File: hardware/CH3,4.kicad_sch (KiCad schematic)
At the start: 104 parts, among them J2 RJ45, J3 RJ45, U10 ADG719, U11 INA828, U12 OPA2192, U13 OPA2192, U14 INA828, U15 SGM2059, U4 INA828, U5 OPA2192, U6 OPA2192, U7 INA828, U8 SGM2059, U9 ADG719

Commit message: feat：远程感测原理图；多路通道
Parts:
- removed C136, C137, C27, C28, C33, C34: 1uF, Capacitor_SMD:C_0603_1608Metric, symbol Device:C
- removed C20, C30: 120pF, Capacitor_SMD:C_0603_1608Metric, symbol Device:C
- removed C21, C22, C24, C25, C26, C29, C31, C35, C36, C37: 100pF, Capacitor_SMD:C_0603_1608Metric, symbol Device:C
- removed C23, C32: 750pF, Capacitor_SMD:C_0603_1608Metric, symbol Device:C
- removed C44, C47, C58, C59, C60, C61, C62, C63, C64, C65, C66, C67, C68, C69, C70, C72, C74, C76, C81, C83: 10uF, Capacitor_SMD:C_0603_1608Metric, symbol Device:C
- removed C45, C46, C48, C49, C50, C51, C52, C53, C54, C55, C56, C57, C71, C73, C75, C77, C78, C79, C80, C82: 100nF, Capacitor_SMD:C_0603_1608Metric, symbol Device:C
- removed J2, J3: RJ45, Connector_RJ:RJ45_Amphenol_54602-x08_Horizontal, symbol Connector:RJ45
- removed R10, R27: 8kR, Resistor_SMD:R_0603_1608Metric, symbol Device:R
- removed R11, R25: 7kR, Resistor_SMD:R_0603_1608Metric, symbol Device:R
- removed R12, R14, R18, R19, R26, R28, R3, R4: 1kR, Resistor_SMD:R_0603_1608Metric, symbol Device:R
- removed R13, R31: 26.7kR, Resistor_SMD:R_0603_1608Metric, symbol Device:R
- removed R15, R16, R29, R30: 49.9R, Resistor_SMD:R_0603_1608Metric, symbol Device:R
- removed R17, R32: 12.4kR, Resistor_SMD:R_0603_1608Metric, symbol Device:R
- removed R20, R5: 120R, Resistor_SMD:R_0603_1608Metric, symbol Device:R
- removed R21, R7: 6.19kR, Resistor_SMD:R_0603_1608Metric, symbol Device:R
- removed R22, R6: 8.45kR, Resistor_SMD:R_0603_1608Metric, symbol Device:R
- removed R23, R8: 2.15kR, Resistor_SMD:R_0603_1608Metric, symbol Device:R
- removed R24, R9: 3.92kR, Resistor_SMD:R_0603_1608Metric, symbol Device:R
- removed U10, U9: ADG719, ProPrj_New Project_2026-05-28_15-29-15_2026-05-30:SOT-23-8_L3.0-W1.7-P0.65-LS2.8-TL, symbol Analog_Switch:ADG619BRTZ-REEL7
- removed U11, U14, U4, U7: INA828, Package_SO:Infineon_PG-DSO-8-43, symbol Amplifier_Instrumentation:INA828IDR
- removed U12, U13, U5, U6: OPA2192, Package_SO:SOIC-8_3.9x4.9mm_P1.27mm, symbol Amplifier_Operational:OPA2192IDR
- removed U15, U8: SGM2059, Package_TO_SOT_SMD:SOT-23-5, symbol Regulator_Linear:SGM2059-ADJXN5G/TR
- added C100, C103, C104, C106, C109, C110, C111, C112, C113, C114, C115, C116, C117, C118, C120, C121, C122, C123, C86, C98: 100nF, Capacitor_SMD:C_0603_1608Metric, symbol Device:C
- added C101, C102, C105, C107, C108, C119, C84, C85, C87, C88, C89, C90, C91, C92, C93, C94, C95, C96, C97, C99: 10uF, Capacitor_SMD:C_0603_1608Metric, symbol Device:C
- added C124, C125: 750pF, Capacitor_SMD:C_0603_1608Metric, symbol Device:C
- added C126, C127, C131, C132, C138, C139: 1uF, Capacitor_SMD:C_0603_1608Metric, symbol Device:C
- added C128, C129, C130, C133, C134, C135, C38, C39, C42, C43: 100pF, Capacitor_SMD:C_0603_1608Metric, symbol Device:C
- added C40, C41: 120pF, Capacitor_SMD:C_0603_1608Metric, symbol Device:C
- added J4, J5: RJ45, Connector_RJ:RJ45_Amphenol_54602-x08_Horizontal, symbol Connector:RJ45
- added R33, R41: 26.7kR, Resistor_SMD:R_0603_1608Metric, symbol Device:R
- added R34, R35, R36, R37, R52, R54, R61, R62: 1kR, Resistor_SMD:R_0603_1608Metric, symbol Device:R
- added R38, R43: 12.4kR, Resistor_SMD:R_0603_1608Metric, symbol Device:R
- added R39, R40: 120R, Resistor_SMD:R_0603_1608Metric, symbol Device:R
- added R42, R44: 6.19kR, Resistor_SMD:R_0603_1608Metric, symbol Device:R
- added R45, R46: 8.45kR, Resistor_SMD:R_0603_1608Metric, symbol Device:R
- added R47, R48: 2.15kR, Resistor_SMD:R_0603_1608Metric, symbol Device:R
- added R49, R50: 3.92kR, Resistor_SMD:R_0603_1608Metric, symbol Device:R
- added R51, R53: 7kR, Resistor_SMD:R_0603_1608Metric, symbol Device:R
- added R55, R56, R59, R60: 49.9R, Resistor_SMD:R_0603_1608Metric, symbol Device:R
- added R57, R58: 8kR, Resistor_SMD:R_0603_1608Metric, symbol Device:R
- added U16, U20, U21, U22: INA828, Package_SO:Infineon_PG-DSO-8-43, symbol Amplifier_Instrumentation:INA828IDR
- added U17, U23: SGM2059, Package_TO_SOT_SMD:SOT-23-5, symbol Regulator_Linear:SGM2059-ADJXN5G/TR
- added U18, U19: ADG719, ProPrj_New Project_2026-05-28_15-29-15_2026-05-30:SOT-23-8_L3.0-W1.7-P0.65-LS2.8-TL, symbol Analog_Switch:ADG619BRTZ-REEL7
- added U24, U25, U26, U27: OPA2192, Package_SO:SOIC-8_3.9x4.9mm_P1.27mm, symbol Amplifier_Operational:OPA2192IDR
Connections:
- net +2.5VA: now also C138.2, C139.2, R34.1, R35.1
- net +4VA: now also C101.2, C102.1, C105.1, C108.1, C110.2, C112.2, C114.2, C115.1, C116.2, C117.2, C118.1, C119.2, C120.2, C121.1, C122.2, C123.1, C84.1, C87.1, C90.1, C92.1, C94.1, C96.1, C98.2, C99.1, U16.7 (+VS), U17.1 (IN), U17.3 (EN), U18.4 (VDD), U19.4 (VDD), U20.7 (+VS), U21.7 (+VS), U22.7 (+VS), U23.1 (IN), U23.3 (EN), U24.4 (VSS), U25.4 (VSS), U26.4 (VSS), U27.4 (VSS)
- net -4VA: now also C100.1, C103.1, C106.1, C109.1, C111.1, C113.1, C85.2, C88.2, C91.2, C93.2, C95.2, C97.2, U16.4 (-VS), U18.7 (VSS), U19.7 (VSS), U20.4 (-VS), U21.4 (-VS), U22.4 (-VS)
- net GND: now also C100.2, C101.1, C102.2, C103.2, C104.1, C105.2, C106.2, C107.1, C108.2, C109.2, C110.1, C111.2, C112.1, C113.2, C114.1, C115.2, C116.1, C117.1, C118.2, C119.1, C120.1, C121.2, C122.1, C123.2, C126.2, C127.2, C128.1, C130.2, C131.2, C132.2, C133.1, C135.2, C138.1, C139.1, C38.2, C39.2, C42.2, C43.2, C84.2, C85.1, C86.1, C87.2, C88.1, C89.1, C90.2, C91.1, C92.2, C93.1, C94.2, C95.1, C96.2, C97.1, C98.1, C99.2, J4.2, J4.7, J5.2, J5.7, R36.2, R37.2, R38.1, R43.1, U16.5 (REF), U17.2 (GND), U18.3 (GND), U19.3 (GND), U20.5 (REF), U23.2 (GND), U24.8 (VDD), U25.8 (VDD), U26.8 (VDD), U27.8 (VDD)
- net V_{REF}: now also C126.1, C127.1, C131.1, C132.1, R52.1, R54.1, U21.5 (REF), U22.5 (REF), U26.5 (VINB+), U27.5 (VINB+)
- new net: C40.2, R42.1, R45.2
- new net: R42.2, U21.6 (OUT)
- new net: R33.1, U16.6 (OUT)
- new net: R39.2, U21.1 (RG)
- new net: U18.1 (D), U21.2 (-IN)
- new net: R39.1, U21.8 (RG)
- new net: R58.1, R62.2, U27.6 (VINB-)
- new net: C38.1, R45.1, U24.3 (VINA+)
- new net: R40.2, U22.1 (RG)
- new net: U19.1 (D), U22.2 (-IN)
- new net: R44.2, U22.6 (OUT)
- new net: R40.1, U22.8 (RG)
- new net: R34.2, R36.1, U18.8 (S2)
- new net: C43.1, R50.1, U25.5 (VINB+)
- new net: C125.1, R53.2, R58.2, U25.6 (VINB-), U25.7 (VOUTB)
- new net: R57.1, R61.2, U26.6 (VINB-)
- new net: C124.1, R51.2, R57.2, U24.6 (VINB-), U24.7 (VOUTB)
- new net: C42.1, R49.1, U24.5 (VINB+)
- new net: R51.1, R52.2, U26.3 (VINA+)
- new net: R41.1, U20.6 (OUT)
- new net: R41.2, R43.2, U23.4 (FB)
- new net: R53.1, R54.2, U27.3 (VINA+)
- new net: C125.2, R48.1, R50.2
- new net: C39.1, R46.1, U25.3 (VINA+)
- new net: C41.2, R44.1, R46.2
- new net: C124.2, R47.1, R49.2
- new net: C41.1, R48.2, U25.1 (VOUTA), U25.2 (VINA-)
- new net: C40.1, R47.2, U24.1 (VOUTA), U24.2 (VINA-)
- new net: R33.2, R38.2, U17.4 (FB)
- new net: R35.2, R37.1, U19.8 (S2)
- new net CH3+: J4.4, U21.3 (+IN)
- new net CH3-: J4.5, U18.2 (S1)
- new net CH4+: J5.4, U22.3 (+IN)
- new net CH4-: J5.5, U19.2 (S1)
- new net Ctrl3: U18.6 (IN)
- new net Ctrl4: U19.6 (IN)
- new net D3Q+: R55.2, U26.1 (VOUTA), U26.2 (VINA-)
- new net D3Q-: R56.2, R61.1, U26.7 (VOUTB)
- new net D4Q+: R59.2, U27.1 (VOUTA), U27.2 (VINA-)
- new net D4Q-: R60.2, R62.1, U27.7 (VOUTB)
- new net EX3+: C86.2, C89.2, J4.1, J4.8, U17.5 (OUT)
- new net EX4+: C104.2, C107.2, J5.1, J5.8, U23.5 (OUT)
- new net OUT3+: C128.2, C129.1, R55.1
- new net OUT3-: C129.2, C130.1, R56.1
- new net OUT4+: C133.2, C134.1, R59.1
- new net OUT4-: C134.2, C135.1, R60.1
- new net RS3+: J4.3, U16.3 (+IN)
- new net RS3-: J4.6, U16.2 (-IN)
- new net RS4+: J5.3, U20.3 (+IN)
- new net RS4-: J5.6, U20.2 (-IN)

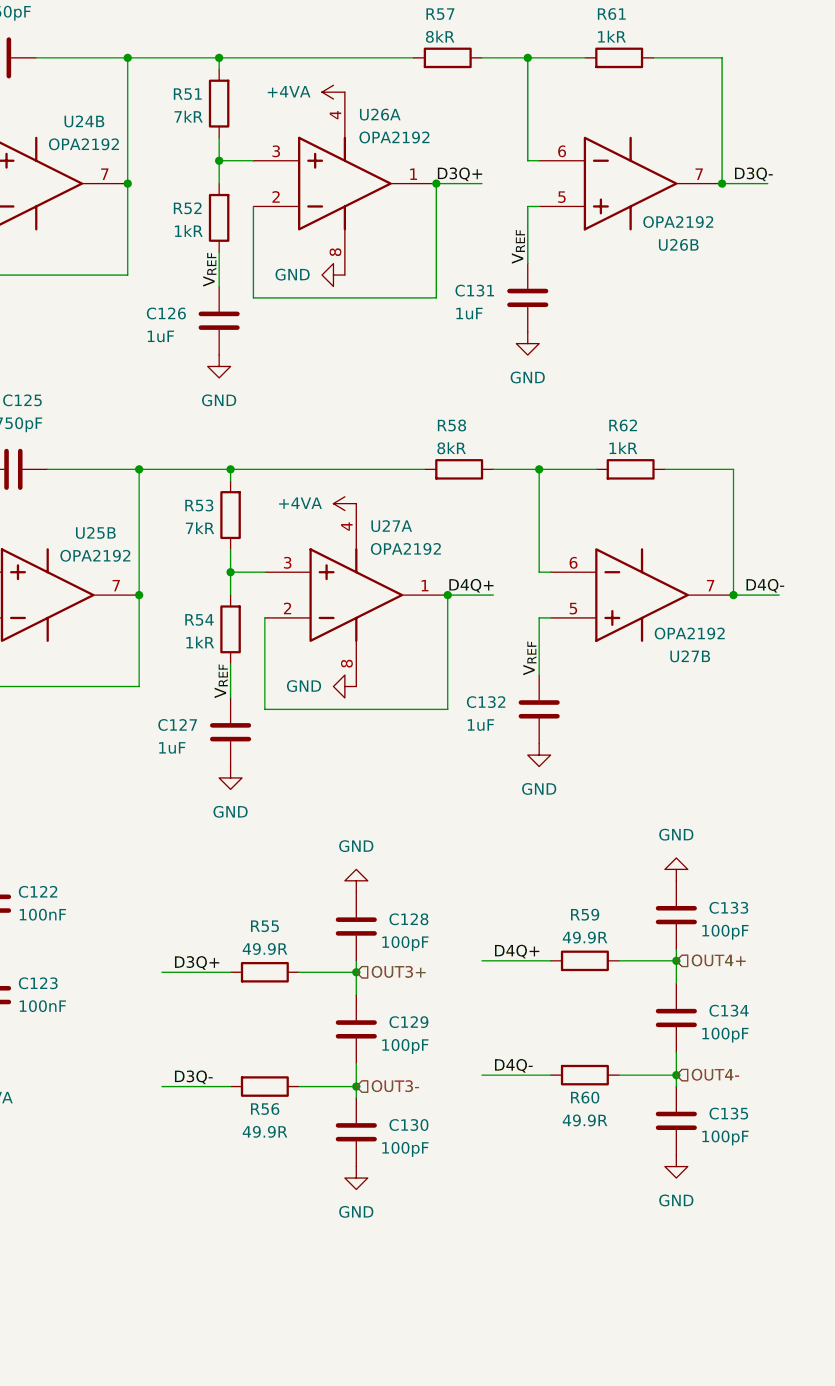
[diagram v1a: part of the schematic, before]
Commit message: feat：输入滤波原理图
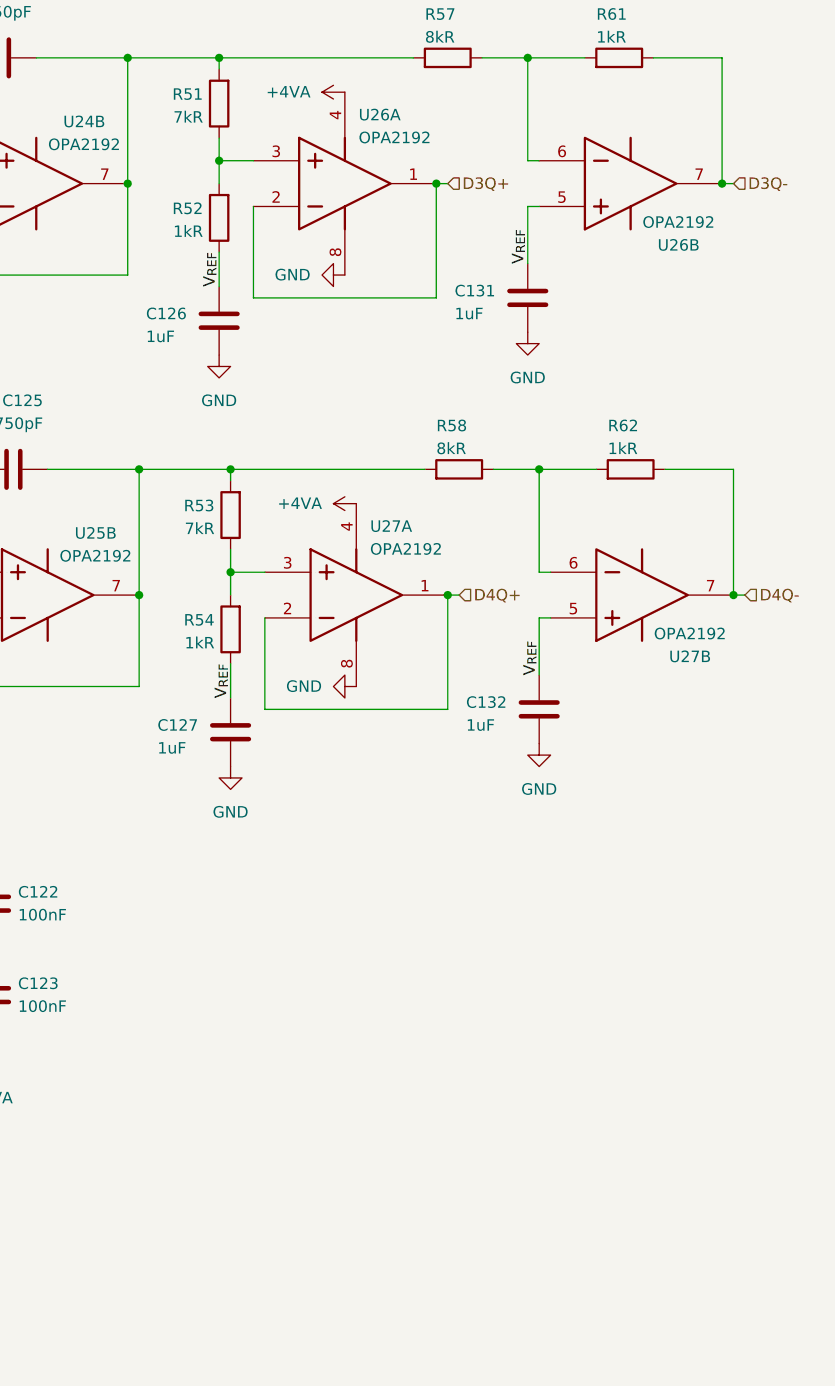
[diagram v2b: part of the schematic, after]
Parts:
- removed C128, C129, C130, C133, C134, C135: 100pF, Capacitor_SMD:C_0603_1608Metric, symbol Device:C
- removed R55, R56, R59, R60: 49.9R, Resistor_SMD:R_0603_1608Metric, symbol Device:R

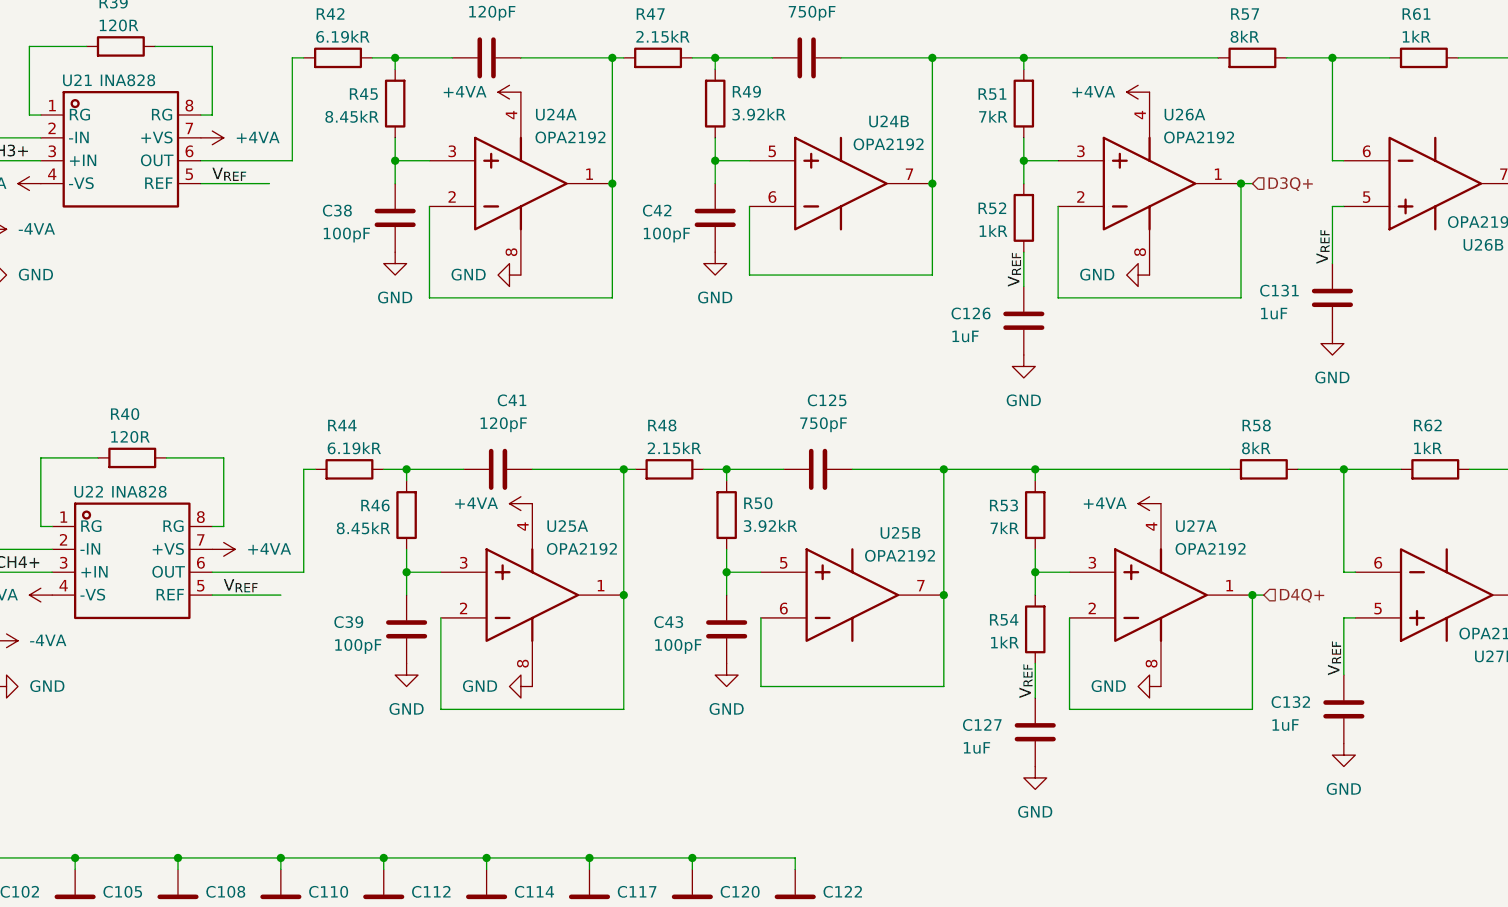
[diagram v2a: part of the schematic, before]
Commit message: feat：电平触发原理图
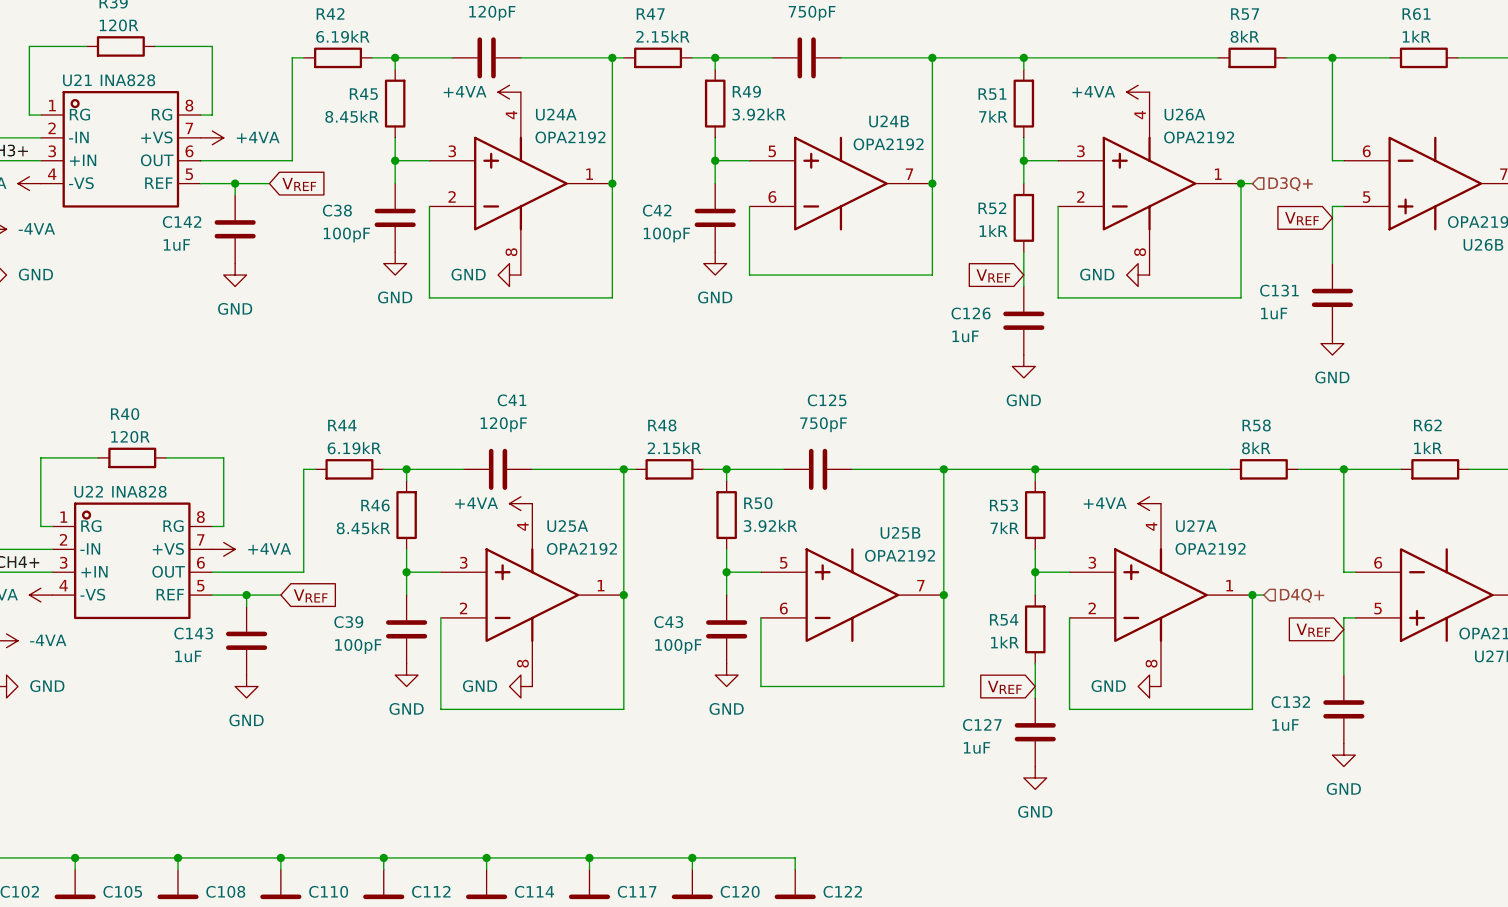
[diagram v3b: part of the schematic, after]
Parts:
- added C142, C143: 1uF, Capacitor_SMD:C_0603_1608Metric, symbol Device:C
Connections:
- net GND: now also C142.2, C143.2
- net V_{REF}: now also C142.1, C143.1

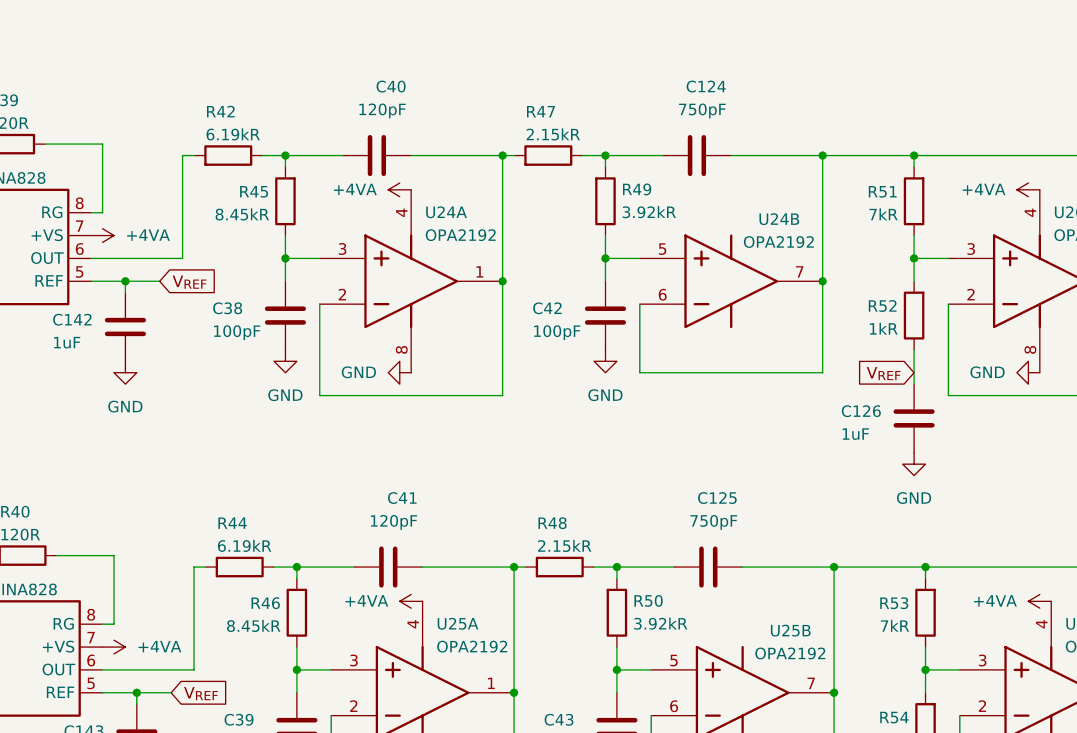
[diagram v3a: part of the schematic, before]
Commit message: feat：模拟前端布线，单片机/SRAM布线
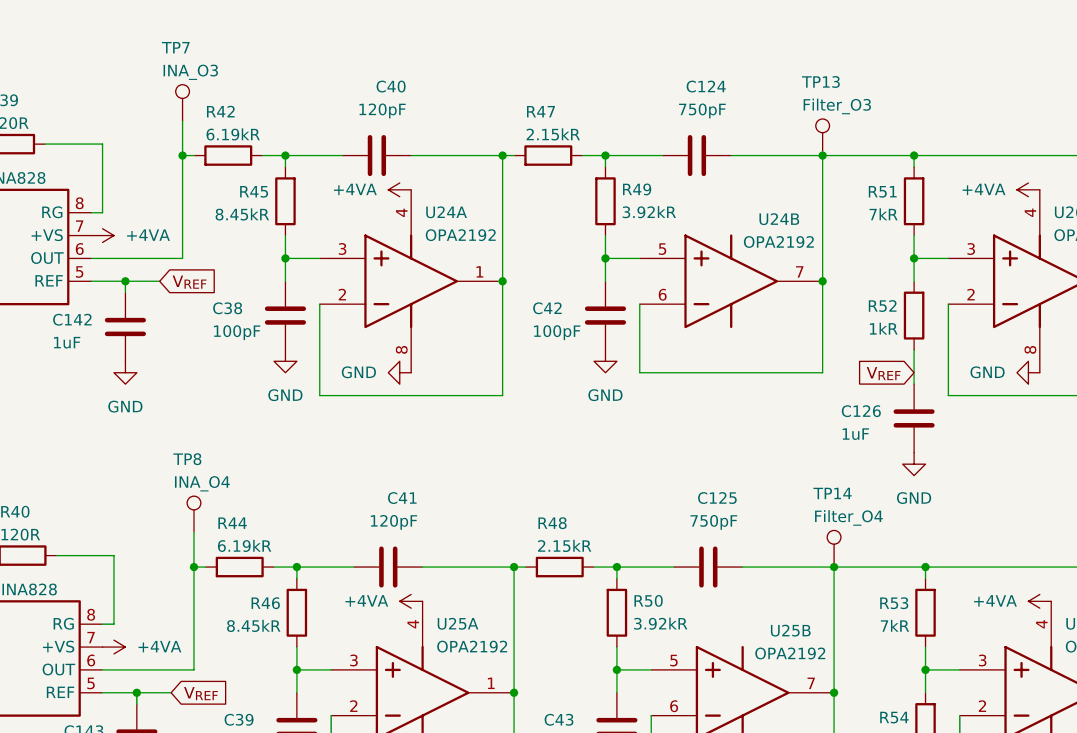
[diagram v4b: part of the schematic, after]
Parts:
- added TP13: Filter_O3, TestPoint:TestPoint_Pad_D1.0mm, symbol Connector:TestPoint
- added TP14: Filter_O4, TestPoint:TestPoint_Pad_D1.0mm, symbol Connector:TestPoint
- added TP7: INA_O3, TestPoint:TestPoint_Pad_D1.0mm, symbol Connector:TestPoint
- added TP8: INA_O4, TestPoint:TestPoint_Pad_D1.0mm, symbol Connector:TestPoint
- U16, U20, U21, U22: footprint Package_SO:Infineon_PG-DSO-8-43 -> Package_SO:SOIC-8_3.9x4.9mm_P1.27mm
- U18, U19: footprint ProPrj_New Project_2026-05-28_15-29-15_2026-05-30:SOT-23-8_L3.0-W1.7-P0.65-LS2.8-TL -> Package_TO_SOT_SMD:SOT-23-8
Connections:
- net at R42.2, U21.6 (OUT): now also TP7.1
- net at R44.2, U22.6 (OUT): now also TP8.1
- net at C125.1, R53.2, R58.2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: now also TP14.1
- net at C124.1, R51.2, R57.2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: now also TP13.1

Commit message: feat：电源部分
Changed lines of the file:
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@@
+		)
+	)
+	(hierarchical_label "Ctrl4"
+		(shape input)
+		(at 64.77 95.25 180)
+		(effects
+			(font
+				(size 1.27 1.27)
+			)
+			(justify right)
 		)
 	)
@@
 		)
 	)
+	(hierarchical_label "Ctrl3"
+		(shape input)
+		(at 63.5 49.53 180)
+		(effects
+			(font
+				(size 1.27 1.27)
+			)
+			(justify right)
+		)
+	)
